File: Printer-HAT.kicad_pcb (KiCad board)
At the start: 2 copper layers, 65 x 56 mm, 38 parts, among them J1 Screw_Terminal, J4 Conn_01x03_Male, K1 SRD-05VDC-SL-C, K2 SLA-05VDC-SL-C, P1 Conn_02x20_Odd_Even, Q2 S8050, Q3 S8050, Q4 Q_Dual_PNP_PNP_C1B1B2C2E2E1, Q5 DMG2305UX-7, U1 LM2596S-5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

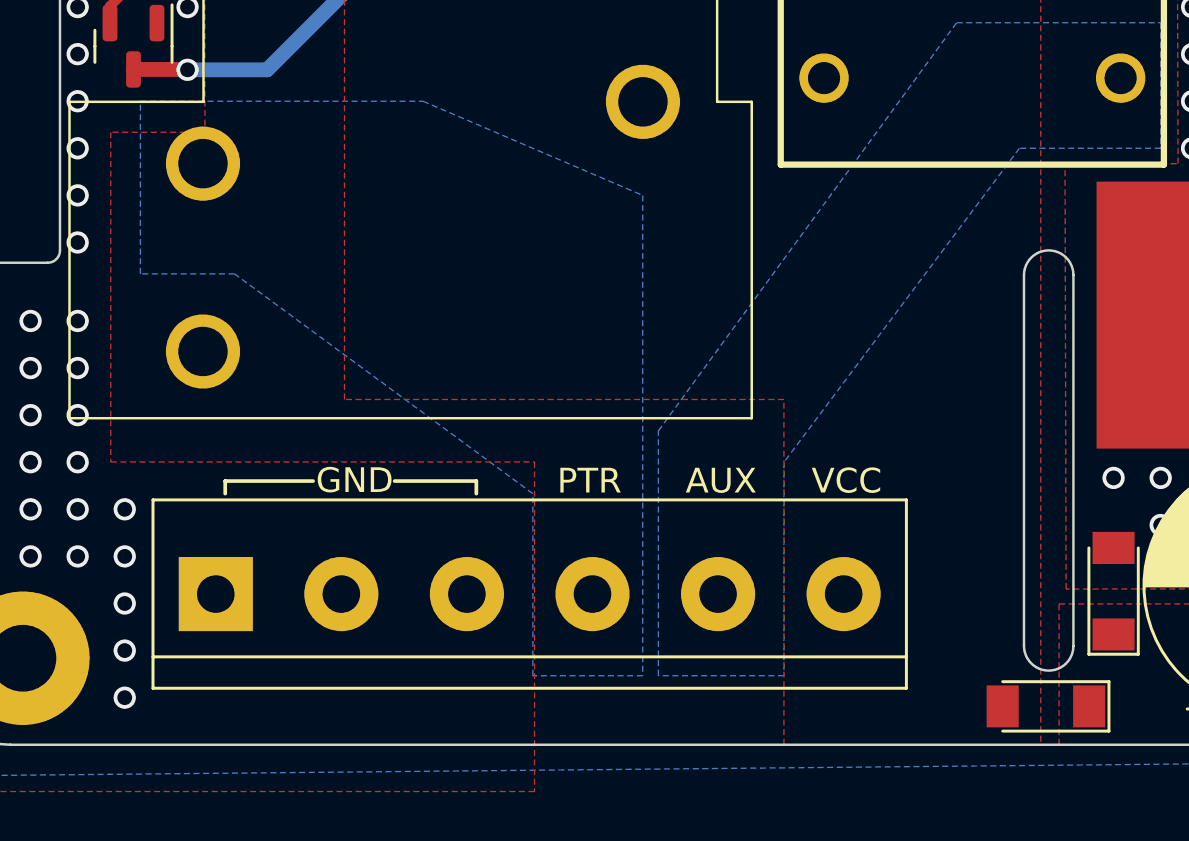
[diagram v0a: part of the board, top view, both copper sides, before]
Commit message: update screw terminal to 5mm pitch
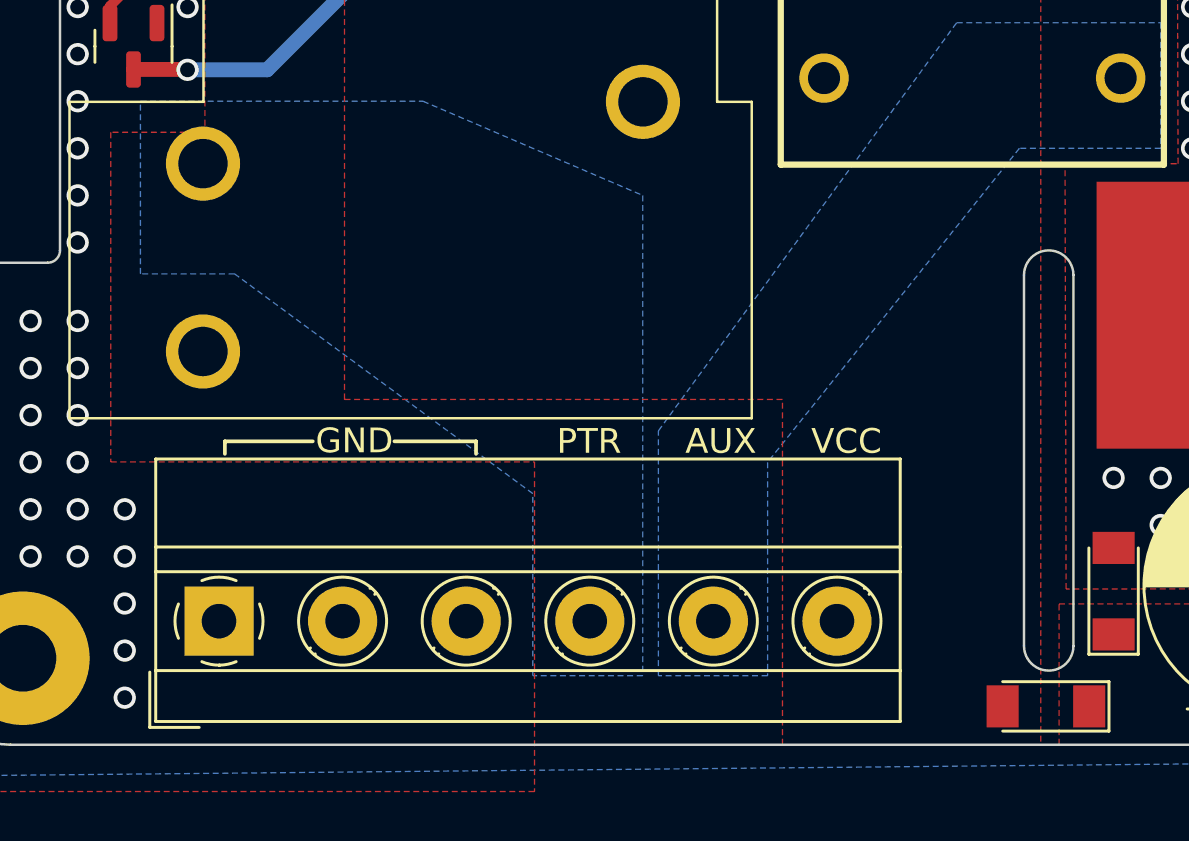
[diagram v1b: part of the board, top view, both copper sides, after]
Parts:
- J1: footprint TerminalBlock:TerminalBlock_bornier-6_P5.08mm -> TerminalBlock_MetzConnect:TerminalBlock_MetzConnect_Type011_RT05506HBWC_1x06_P5.00mm_Horizontal
- moved J1 1.10 mm to (211.4, 145.0)
